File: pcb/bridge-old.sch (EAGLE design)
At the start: 38 parts, among them IC2 LM358D, IC3 78L05SMD, X1 PN61729-S

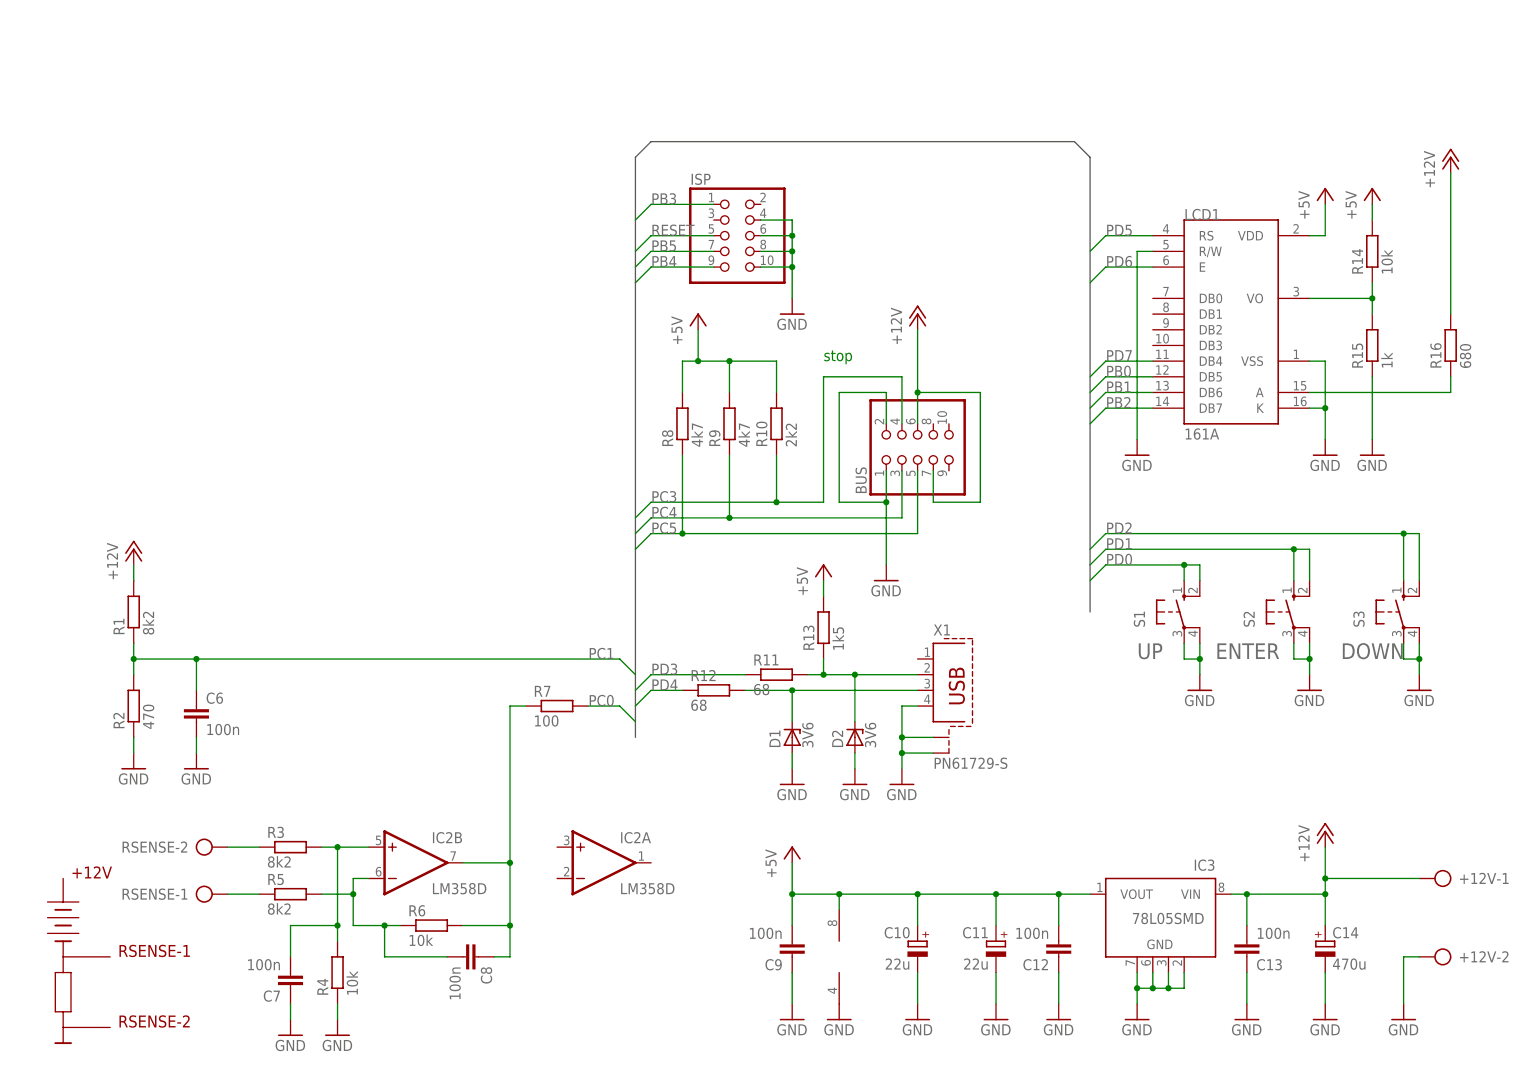
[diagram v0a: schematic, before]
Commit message: Rename 'bridge' project. Create board for new bridge.
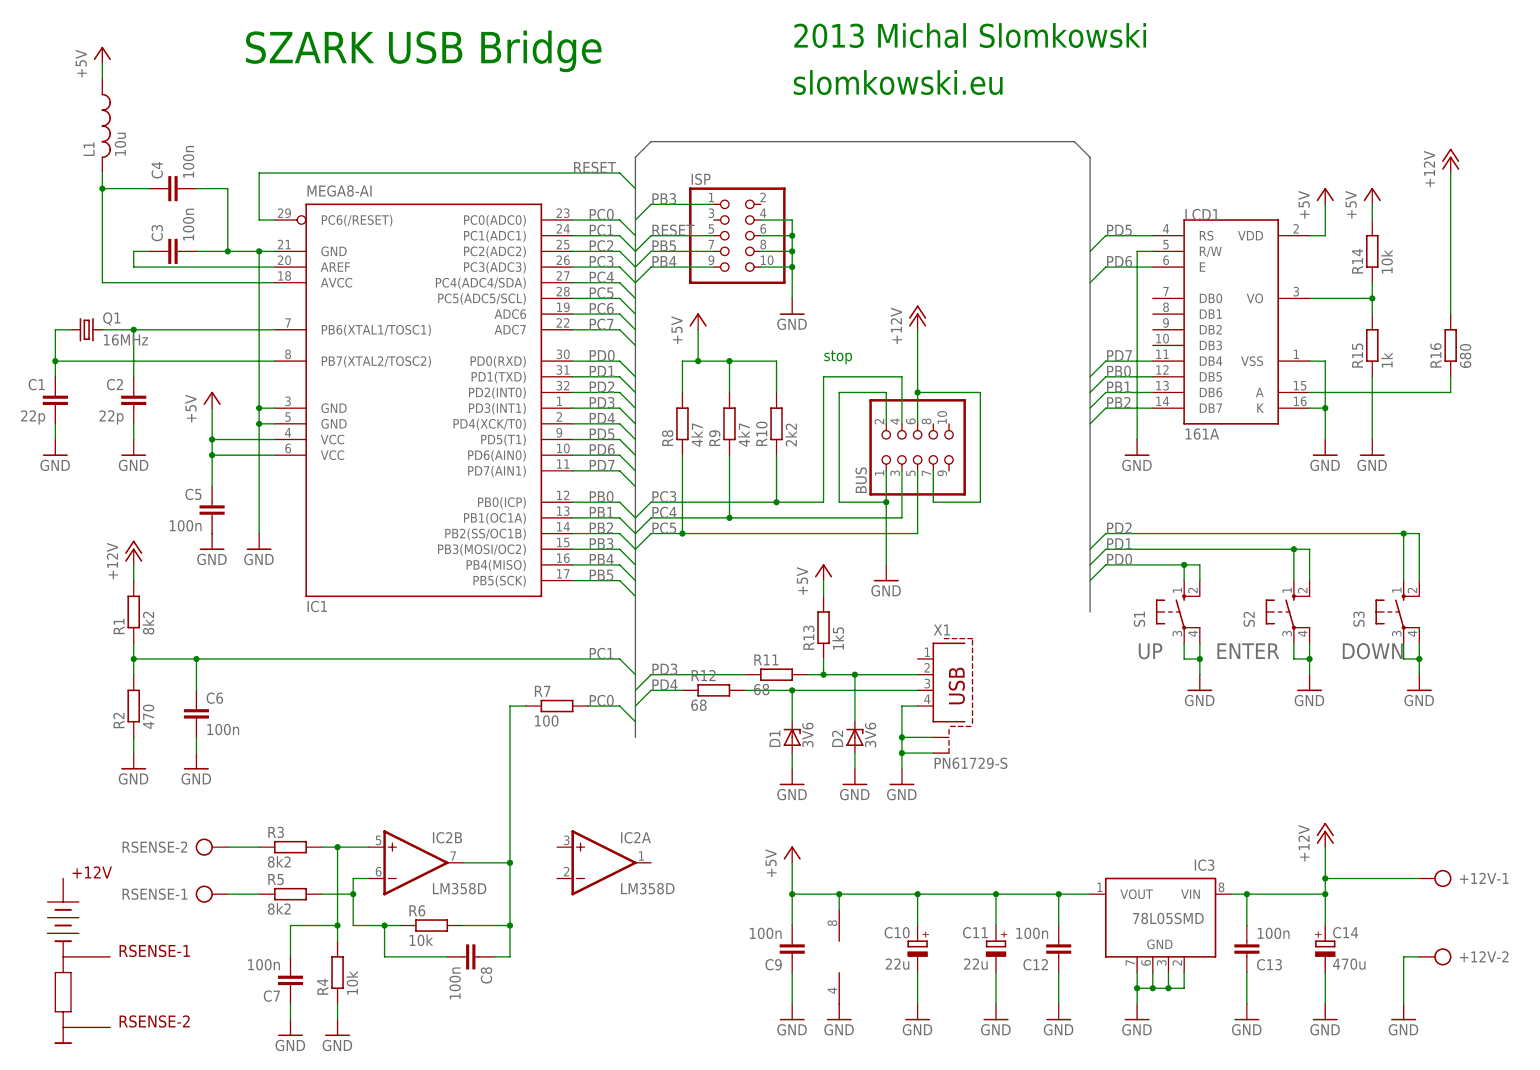
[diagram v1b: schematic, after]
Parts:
- added C1, C2: 22p, rcl:C-EUC1206
- added C3, C4, C5: 100n, rcl:C-EUC1206
- added IC1: MEGA8-AI, atmel:MEGA8-AI
- added L1: 10u, rcl:L-USL1812
- added Q1: 16MHz, crystal:CRYSTALHC49UP
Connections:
- new net N$10: C4.1, IC1.AVCC, L1.2
- new net N$11: C1.1, IC1.PB7(XTAL2/TOSC2), Q1.1
- new net N$8: C3.1, IC1.AREF
- new net N$9: C2.1, IC1.PB6(XTAL1/TOSC1), Q1.2
- new net PC2: IC1.PC2(ADC2)
- new net PC6: IC1.ADC6
- new net PC7: IC1.ADC7
- net +5V: now also C5.1, IC1.VCC@1, IC1.VCC@2, L1.1
- net GND: now also C1.2, C2.2, C3.2, C4.2, C5.2, IC1.GND, IC1.GND@1, IC1.GND@2
- net PB0: now also IC1.PB0(ICP)
- net PB1: now also IC1.PB1(OC1A)
- net PB2: now also IC1.PB2(SS/OC1B)
- net PB3: now also IC1.PB3(MOSI/OC2)
- net PB4: now also IC1.PB4(MISO)
- net PB5: now also IC1.PB5(SCK)
- net PC0: now also IC1.PC0(ADC0)
- net PC1: now also IC1.PC1(ADC1)
- net PC3: now also IC1.PC3(ADC3)
- net PC4: now also IC1.PC4(ADC4/SDA)
- net PC5: now also IC1.PC5(ADC5/SCL)
- net PD0: now also IC1.PD0(RXD)
- net PD1: now also IC1.PD1(TXD)
- net PD2: now also IC1.PD2(INT0)
- net PD3: now also IC1.PD3(INT1)
- net PD4: now also IC1.PD4(XCK/T0)
- net PD5: now also IC1.PD5(T1)
- net PD6: now also IC1.PD6(AIN0)
- net PD7: now also IC1.PD7(AIN1)
- net RESET: now also IC1.PC6(/RESET)
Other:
- note added: "2013 Michal Slomkowski"
- note added: "SZARK USB Bridge"
- note added: "slomkowski.eu"
